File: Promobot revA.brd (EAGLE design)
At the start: 184.5 x 171.4 mm, 450 parts, among them J3 USB-MICRO!!!, J4 3x2M, M1OUTA MOUNTINGHOLE2.5_THICK, M1OUTA1 MOUNTINGHOLE2.5_THICK, M1OUTA10 MOUNTINGHOLE2.5_THICK, M1OUTA11 MOUNTINGHOLE2.5_THICK, M1OUTA12 MOUNTINGHOLE2.5_THICK, M1OUTA13 MOUNTINGHOLE2.5_THICK, M1OUTA14 MOUNTINGHOLE2.5_THICK, M1OUTA15 MOUNTINGHOLE2.5_THICK, M1OUTA16 MOUNTINGHOLE2.5_THICK, M1OUTA17 MOUNTINGHOLE2.5_THICK, M1OUTA18 MOUNTINGHOLE2.5_THICK, M1OUTA19 MOUNTINGHOLE2.5_THICK, M1OUTA2 MOUNTINGHOLE2.5_THICK, M1OUTA20 MOUNTINGHOLE2.5_THICK, M1OUTA21 MOUNTINGHOLE2.5_THICK, M1OUTA22 MOUNTINGHOLE2.5_THICK, M1OUTA23 MOUNTINGHOLE2.5_THICK, M1OUTA24 MOUNTINGHOLE2.5_THICK, M1OUTA25 MOUNTINGHOLE2.5_THICK, M1OUTA3 MOUNTINGHOLE2.5_THICK, M1OUTA4 MOUNTINGHOLE2.5_THICK, M1OUTA5 MOUNTINGHOLE2.5_THICK, M1OUTA6 MOUNTINGHOLE2.5_THICK, M1OUTA7 MOUNTINGHOLE2.5_THICK, M1OUTA8 MOUNTINGHOLE2.5_THICK, M1OUTA9 MOUNTINGHOLE2.5_THICK, M1OUTB MOUNTINGHOLE2.5_THICK, M1OUTB1 MOUNTINGHOLE2.5_THICK, M1OUTB2 MOUNTINGHOLE2.5_THICK, M1OUTB3 MOUNTINGHOLE2.5_THICK, M1OUTB4 MOUNTINGHOLE2.5_THICK, M1OUTB5 MOUNTINGHOLE2.5_THICK, Q1 IPB80N03S4L-03, Q2 IPB80N03S4L-03, Q3 IPB80N03S4L-03, Q4 IPB80N03S4L-03, Q6 CSD86330Q3D, Q7 CSD86330Q3D, T1 FDN340P/PMV48XP, T2 PMV48XP, U1 VNH5019A-E, U10 ATMEGA32U4-XUMU, U11 NCP1117-5, U12 TPS563200, U2 ACS714, U3 VNH5019A-E, U4 ACS714, U5 VNH5019A-E, U6 ACS714, U7 VNH5019A-E, U8 ACS714, U9 LP2985-33DBVR, X1 MKS1852-6-0-202, X10 MKS1852-6-0-202, X11 MKS1852-6-0-202, X12 MKS1852-6-0-202, X13 MKS1852-6-0-202, X14 MKS1852-6-0-202, X15 MKS1852-6-0-202, X16 MKS1852-6-0-202, X17 MKS1852-6-0-202, X18 MKS1852-6-0-202, X19 MKS1852-6-0-202, X2 MKS1852-6-0-202, X20 MKS1852-6-0-202, X21 MKS1852-6-0-202, X22 MKS1852-6-0-202, X23 MKS1852-6-0-202, X24 MKS1852-6-0-202, X3 RC-5231, X4 RC-5231, X5 MKS1852-6-0-202, X6 MKS1852-6-0-202, X7 MKS1852-6-0-202, X8 MKS1852-6-0-202, X9 MKS1852-6-0-202, Y3 16MHz KX-7

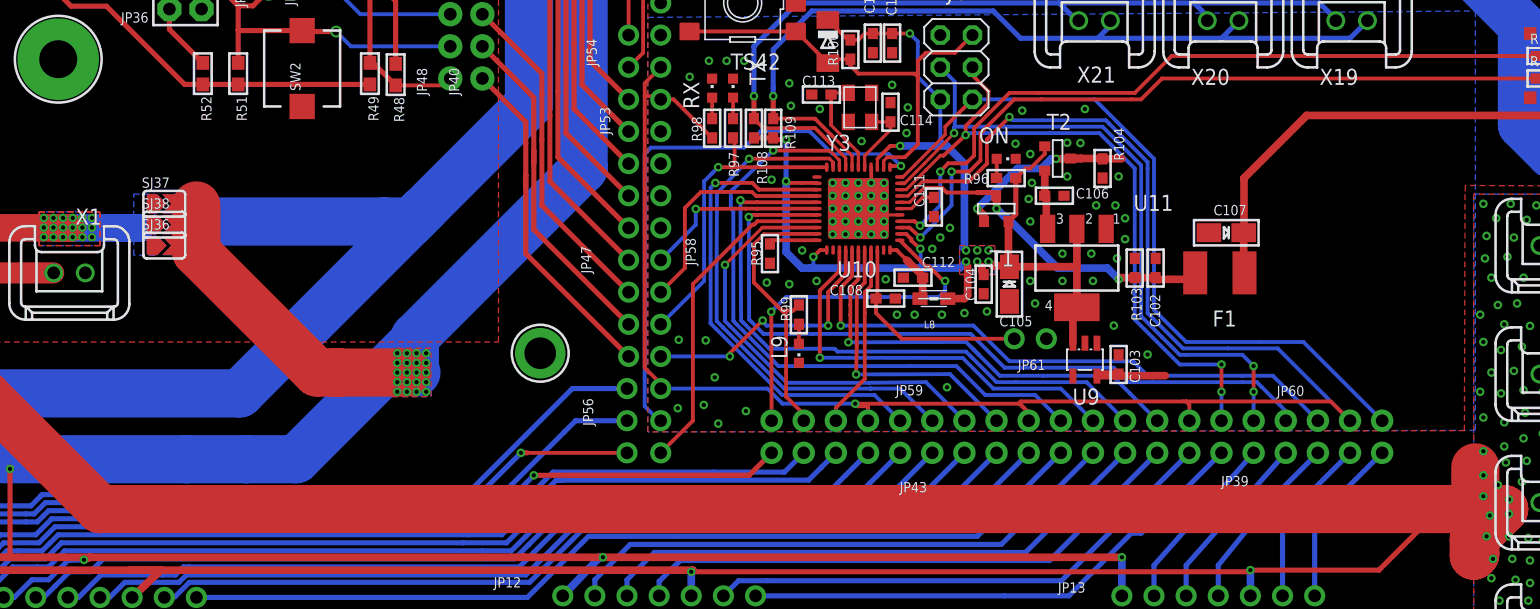
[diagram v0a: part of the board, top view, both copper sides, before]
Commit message: Add voltage divider
R110, R111 - voltage divider. Connected to A5 pin
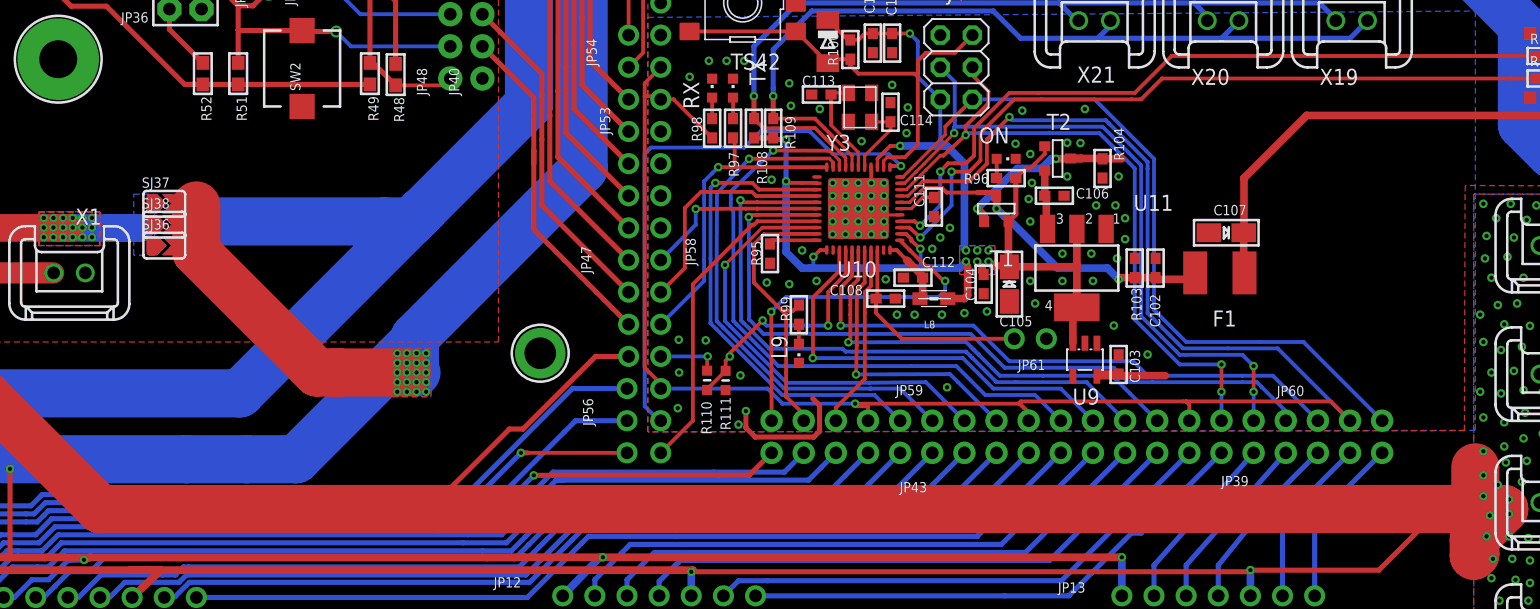
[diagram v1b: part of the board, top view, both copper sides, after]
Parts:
- added R110: 3k, microbuilder:_0603MP
- added R111: 1k, microbuilder:_0603MP
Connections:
- removed net N$99: JP40.1, JP47.1
- new net VBAT: JP58.4, R110.2
- net A1: now also R110.1, R111.1; no longer JP58.4
- net GND: now also R111.2
- net MAINVCC: now also JP47.1
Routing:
- net N$99: track 27.8 -> 0.00 mm
- net MAINVCC: track 400.8 -> 421.4 mm
- net GND: track 5.65 -> 16.1 mm
- net VBAT: track 0.00 -> 4.85 mm, vias 0 -> 1
- net A1: track 21.3 -> 19.2 mm
- net A0: track 32.8 -> 33.6 mm
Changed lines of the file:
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@@
 <setting verticaltext="up"/>
 </settings>
-<grid distance="0.1" unitdist="mm" unit="mm" style="lines" multiple="1" display="yes" altdistance="0.025" altunitdist="inch" altunit="inch"/>
+<grid distance="1" unitdist="mil" unit="mil" style="lines" multiple="1" display="yes" altdistance="0.025" altunitdist="inch" altunit="inch"/>
 <layers>
 <layer number="1" name="Top" color="4" fill="1" visible="yes" active="yes"/>
@@
 <layer number="17" name="Pads" color="2" fill="1" visible="yes" active="yes"/>
 <layer number="18" name="Vias" color="2" fill="1" visible="yes" active="yes"/>
-<layer number="19" name="Unrouted" color="6" fill="1" visible="no" active="yes"/>
+<layer number="19" name="Unrouted" color="6" fill="1" visible="yes" active="yes"/>
 <layer number="20" name="Dimension" color="15" fill="1" visible="no" active="yes"/>
 <layer number="21" name="tPlace" color="7" fill="1" visible="yes" active="yes"/>
@@
 <element name="M1OUTA24" library="microbuilder" package="MOUNTINGHOLE_2.5_PLATED_THICK" value="MOUNTINGHOLE2.5_THICK" x="129.54" y="55.499" smashed="yes"/>
 <element name="M1OUTA25" library="microbuilder" package="MOUNTINGHOLE_2.5_PLATED_THICK" value="MOUNTINGHOLE2.5_THICK" x="97.79" y="80.264" smashed="yes"/>
+<element name="R110" library="microbuilder" package="_0603MP" value="3k" x="110.9818" y="78.1248" smashed="yes" rot="R90">
+<attribute name="NAME" x="111.3374" y="73.8449" size="0.8128" layer="25" ratio="18" rot="R90"/>
+<attribute name="VALUE" x="111.9343" y="77.1723" size="0.4064" layer="27" ratio="10" rot="R90"/>
+</element>
+<element name="R111" library="microbuilder" package="_0603MP" value="1k" x="112.4412" y="78.1106" smashed="yes" rot="R270">
+<attribute name="NAME" x="112.0348" y="76.8025" size="0.8128" layer="25" ratio="18" rot="R270"/>
+<attribute name="VALUE" x="111.4887" y="79.0631" size="0.4064" layer="27" ratio="10" rot="R270"/>
+</element>
 </elements>
 <signals>
@@
 <wire x1="183.134" y1="99.695" x2="181.2544" y2="99.695" width="0.6096" layer="1"/>
 <wire x1="181.2544" y1="99.695" x2="180.4416" y2="100.5078" width="0.6096" layer="1"/>
-<via x="110.7186" y="76.1746" extent="1-16" drill="0.3302"/>
-<via x="111.5822" y="78.359" extent="1-16" drill="0.3302"/>
+<via x="108.7628" y="78.74" extent="1-16" drill="0.3302"/>
+<via x="113.6142" y="78.5114" extent="1-16" drill="0.3302"/>
 <via x="108.7374" y="81.3308" extent="1-16" drill="0.3302"/>
 <via x="108.6612" y="75.9206" extent="1-16" drill="0.3302"/>
-<via x="111.8616" y="74.7014" extent="1-16" drill="0.3302"/>
+<via x="113.4618" y="74.6252" extent="1-16" drill="0.3302"/>
 <via x="129.9464" y="77.5716" extent="1-16" drill="0.3302"/>
 <via x="143.129" y="82.4484" extent="1-16" drill="0.3302"/>
 <via x="145.796" y="80.1624" extent="1-16" drill="0.3302"/>
+<contactref element="R111" pad="2"/>
+<wire x1="114.046" y1="75.692" x2="114.046" y2="74.3712" width="0.4064" layer="1"/>
+<wire x1="114.046" y1="74.3712" x2="114.7826" y2="73.6346" width="0.4064" layer="1"/>
+<wire x1="114.7826" y1="73.6346" x2="119.4054" y2="73.6346" width="0.4064" layer="1"/>
+<wire x1="119.4054" y1="73.6346" x2="119.8626" y2="74.0918" width="0.4064" layer="1"/>
+<wire x1="119.8626" y1="74.0918" x2="119.8626" y2="76.1492" width="0.4064" layer="1"/>
+<wire x1="119.8626" y1="76.1492" x2="119.3292" y2="76.6826" width="0.4064" layer="1"/>
 <wire x1="180.4416" y1="104.3178" x2="180.4416" y2="105.4862" width="0" layer="19" extent="1-1"/>
 <wire x1="124.849" y1="91.194" x2="124.968" y2="90.678" width="0" layer="19" extent="1-1"/>
-<wire x1="114.046" y1="75.692" x2="118.237" y2="79.514" width="0" layer="19" extent="1-1"/>
 </signal>
 <signal name="+5V">
@@
 <wire x1="121.936" y1="88.419" x2="121.936" y2="86.5284" width="0.3048" layer="1"/>
 <wire x1="121.936" y1="86.5284" x2="121.158" y2="85.725" width="0.3048" layer="1"/>
-<contactref element="JP58" pad="4"/>
 <wire x1="121.158" y1="85.725" x2="121.031" y2="85.598" width="0.3048" layer="1"/>
 <wire x1="121.031" y1="85.598" x2="120.5484" y2="85.09" width="0.3048" layer="1"/>
@@
 <via x="120.5484" y="82.4484" extent="1-16" drill="0.3302"/>
 <via x="115.3668" y="82.8548" extent="1-16" drill="0.3302"/>
-<wire x1="112.776" y1="80.01" x2="107.315" y2="80.01" width="0.3048" layer="16"/>
 <wire x1="120.5484" y1="82.4484" x2="115.6716" y2="82.4484" width="0.3048" layer="16"/>
 <via x="112.776" y="80.01" extent="1-16" drill="0.3302"/>
@@
 <wire x1="115.3668" y1="82.8548" x2="112.776" y2="80.264" width="0.3048" layer="1"/>
 <wire x1="112.776" y1="80.264" x2="112.776" y2="80.01" width="0.3048" layer="1"/>
+<contactref element="R110" pad="1"/>
+<contactref element="R111" pad="1"/>
+<wire x1="112.4412" y1="78.8726" x2="112.4412" y2="79.6752" width="0.3048" layer="1"/>
+<wire x1="112.4412" y1="79.6752" x2="112.776" y2="80.01" width="0.3048" layer="1"/>
+<wire x1="110.9818" y1="77.3628" x2="110.9818" y2="77.4132" width="0.3048" layer="1"/>
+<wire x1="110.9818" y1="77.4132" x2="112.4412" y2="78.8726" width="0.3048" layer="1"/>
 </signal>
 <signal name="A0">
 <contactref element="U10" pad="36"/>
 <wire x1="121.436" y1="88.419" x2="121.436" y2="86.765" width="0.3048" layer="1"/>
+<wire x1="121.436" y1="86.765" x2="119.888" y2="85.217" width="0.3048" layer="1"/>
+<wire x1="119.35" y1="84.679" x2="119.888" y2="85.217" width="0.3048" layer="1"/>
 <contactref element="JP60" pad="1"/>
-<via x="119.888" y="79.9084" extent="1-16" drill="0.3302"/>
-<wire x1="141.478" y1="74.93" x2="139.446" y2="76.962" width="0.3048" layer="16"/>
-<wire x1="139.446" y1="76.962" x2="138.938" y2="77.47" width="0.3048" layer="16"/>
+<wire x1="141.478" y1="74.93" x2="138.938" y2="77.47" width="0.3048" layer="16"/>
 <wire x1="138.938" y1="77.47" x2="133.604" y2="77.47" width="0.3048" layer="16"/>
-<wire x1="119.888" y1="79.9084" x2="131.191" y2="79.883" width="0.3048" layer="16"/>
-<wire x1="131.191" y1="79.883" x2="133.604" y2="77.47" width="0.3048" layer="16"/>
-<wire x1="121.436" y1="86.765" x2="119.888" y2="85.217" width="0.3048" layer="1"/>
-<wire x1="119.888" y1="85.217" x2="119.888" y2="79.9084" width="0.3048" layer="1"/>
+<wire x1="133.604" y1="77.47" x2="131.191" y2="79.883" width="0.3048" layer="16"/>
+<wire x1="131.191" y1="79.883" x2="119.3292" y2="79.883" width="0.3048" layer="16"/>
+<via x="119.3292" y="79.883" extent="1-16" drill="0.3302"/>
+<wire x1="119.3292" y1="79.883" x2="119.35" y2="79.9038" width="0.3048" layer="1"/>
+<wire x1="119.35" y1="79.9038" x2="119.35" y2="84.679" width="0.3048" layer="1"/>
 </signal>
 <signal name="A4">
@@
 <wire x1="113.8" y1="92.194" x2="113.6142" y2="92.3544" width="0.3048" layer="1"/>
 <wire x1="113.8428" y1="82.677" x2="115.9002" y2="80.6196" width="0.3048" layer="16"/>
-<wire x1="115.9002" y1="80.6196" x2="121.0564" y2="80.6196" width="0.3048" layer="16"/>
-<wire x1="121.0564" y1="80.6196" x2="121.285" y2="80.391" width="0.3048" layer="16"/>
-<wire x1="121.285" y1="80.391" x2="122.4534" y2="80.391" width="0.3048" layer="16"/>
+<wire x1="115.9002" y1="80.6196" x2="121.6914" y2="80.6196" width="0.3048" layer="16"/>
+<wire x1="121.6914" y1="80.6196" x2="121.92" y2="80.391" width="0.3048" layer="16"/>
+<wire x1="121.92" y1="80.391" x2="122.4534" y2="80.391" width="0.3048" layer="16"/>
 <wire x1="122.4534" y1="80.391" x2="131.445" y2="80.391" width="0.3048" layer="16"/>
 <wire x1="131.445" y1="80.391" x2="131.7625" y2="80.0735" width="0.3048" layer="16"/>
@@
 <wire x1="60.198" y1="64.643" x2="58.928" y2="63.373" width="0.4064" layer="16"/>
 </signal>
-<signal name="N$99">
-<contactref element="JP47" pad="1"/>
-<contactref element="JP40" pad="1"/>
-<wire x1="93.218" y1="101.981" x2="96.647" y2="98.552" width="0.4064" layer="1"/>
-<wire x1="96.647" y1="98.552" x2="96.647" y2="96.901" width="0.4064" layer="1"/>
-<wire x1="96.647" y1="96.901" x2="96.647" y2="94.361" width="0.4064" layer="1"/>
-<wire x1="96.647" y1="94.361" x2="96.647" y2="93.345" width="0.4064" layer="1"/>
-<wire x1="104.775" y1="80.01" x2="96.647" y2="88.138" width="0.4064" layer="1"/>
-<wire x1="96.647" y1="88.138" x2="96.647" y2="94.361" width="0.4064" layer="1"/>
-</signal>
 <signal name="N$113">
 <contactref element="JP47" pad="2"/>
@@
 <wire x1="53.848" y1="77.089" x2="50.927" y2="77.089" width="3.81" layer="16"/>
 <wire x1="53.848" y1="77.089" x2="74.041" y2="77.089" width="3.81" layer="16"/>
-<wire x1="168.91" y1="67.945" x2="62.992" y2="67.945" width="3.81" layer="1"/>
+<wire x1="168.91" y1="67.945" x2="89.789" y2="67.945" width="3.81" layer="1"/>
+<wire x1="89.789" y1="67.945" x2="62.992" y2="67.945" width="3.81" layer="1"/>
 <wire x1="62.992" y1="67.945" x2="53.975" y2="76.962" width="3.81" layer="1"/>
 <wire x1="53.975" y1="76.962" x2="51.054" y2="76.962" width="3.81" layer="1"/>
@@
 <wire x1="153.924" y1="63.119" x2="153.797" y2="62.992" width="0.4064" layer="1"/>
 <wire x1="153.797" y1="62.992" x2="109.728" y2="62.992" width="0.4064" layer="1"/>
+<contactref element="JP47" pad="1"/>
+<wire x1="104.775" y1="80.01" x2="102.1588" y2="80.01" width="0.4064" layer="1"/>
+<wire x1="102.1588" y1="80.01" x2="96.4184" y2="74.2696" width="0.4064" layer="1"/>
+<wire x1="96.4184" y1="74.2696" x2="95.3516" y2="74.2696" width="0.4064" layer="1"/>
+<wire x1="95.3516" y1="74.2696" x2="89.662" y2="68.58" width="0.4064" layer="1"/>
+<wire x1="89.662" y1="68.58" x2="89.662" y2="68.072" width="0.4064" layer="1"/>
+<wire x1="89.662" y1="68.072" x2="89.789" y2="67.945" width="0.4064" layer="1"/>
 </signal>
 <signal name="MAINGND">
@@
 <contactref element="JP58" pad="14"/>
 </signal>
+<signal name="VBAT">
+<contactref element="R110" pad="2"/>
+<contactref element="JP58" pad="4"/>
+<wire x1="107.315" y1="80.01" x2="111.0234" y2="80.01" width="0.3048" layer="16"/>
+<via x="111.0234" y="80.01" extent="1-16" drill="0.3302"/>
+<wire x1="111.0234" y1="80.01" x2="110.9818" y2="79.9684" width="0.3048" layer="1"/>
+<wire x1="110.9818" y1="79.9684" x2="110.9818" y2="78.8868" width="0.3048" layer="1"/>
+</signal>
 </signals>
